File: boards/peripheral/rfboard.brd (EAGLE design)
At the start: 30 x 60 mm, 30 parts, among them Q1 IRLML5203, Q2 IRLML5203, Q3 IRLML5203, Q4 IRLML5203, Q5 IRLML5203

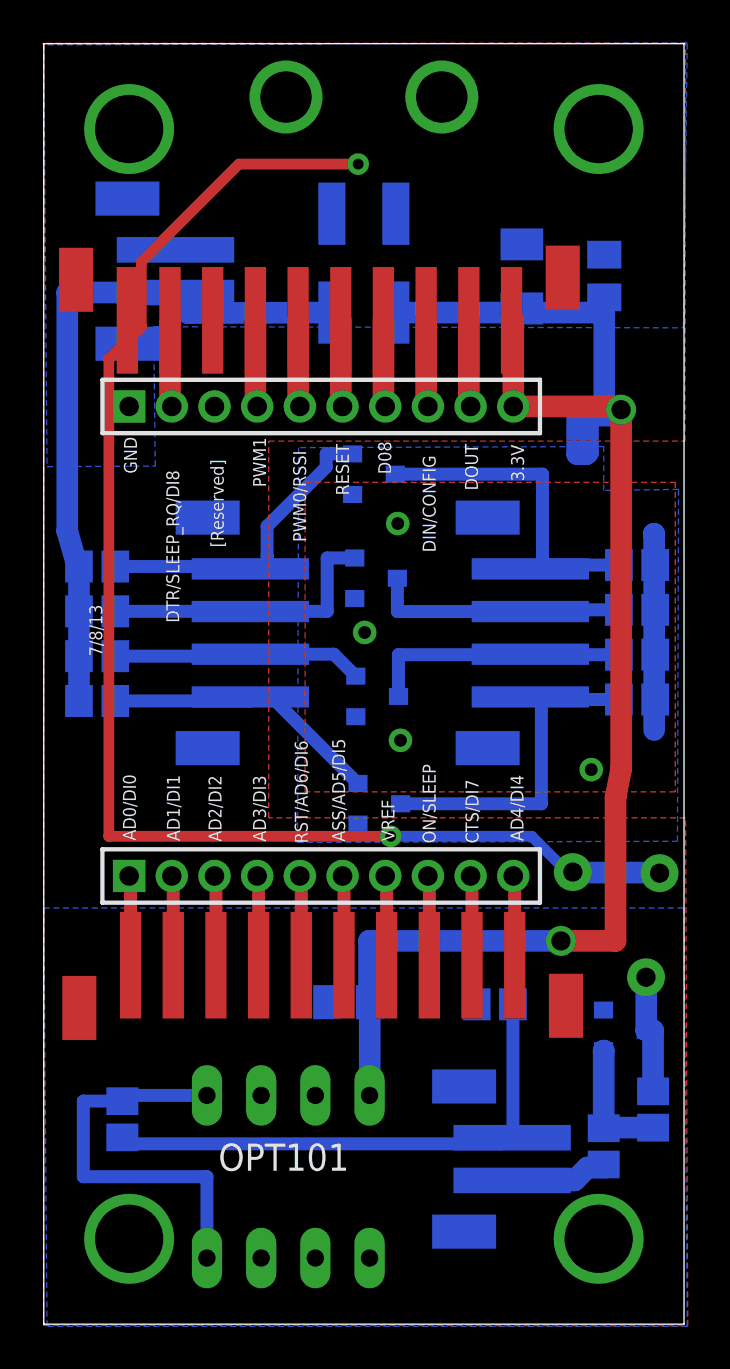
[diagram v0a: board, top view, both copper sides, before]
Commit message: Changing boards for fet and text improvements
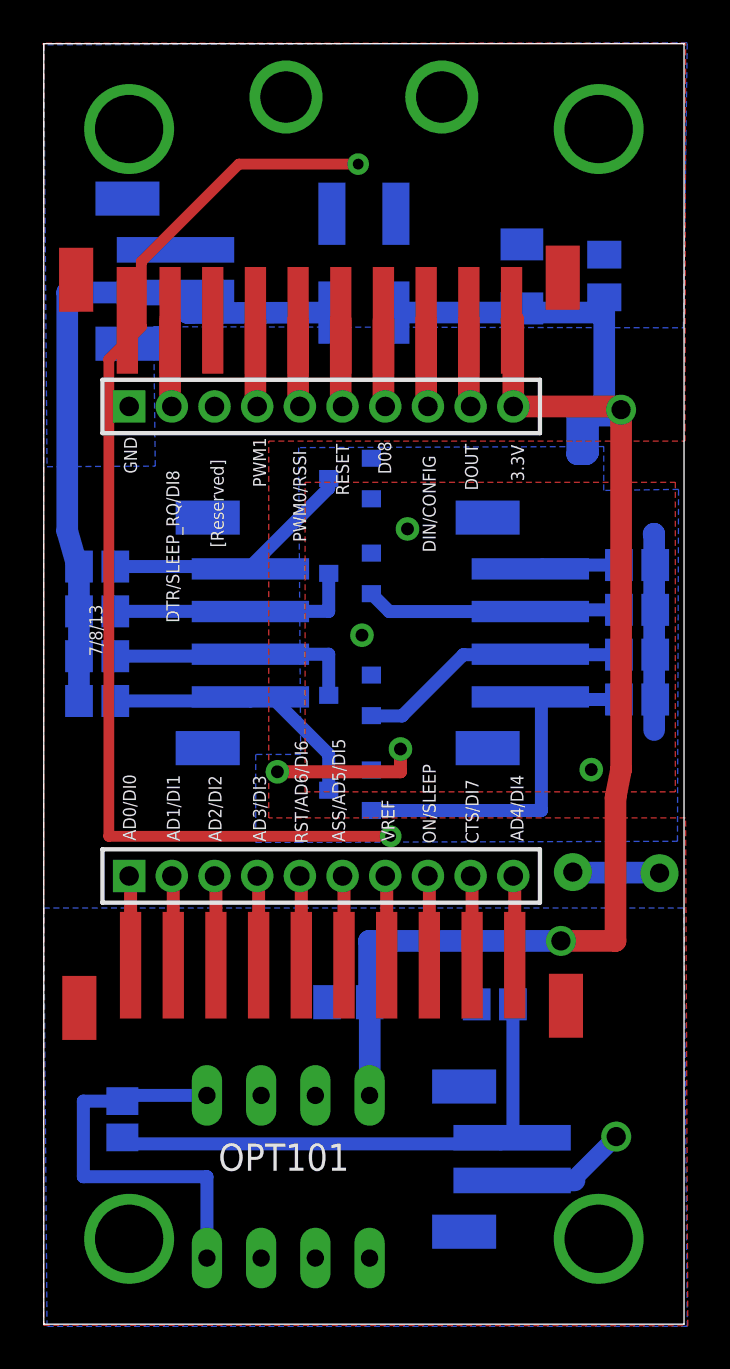
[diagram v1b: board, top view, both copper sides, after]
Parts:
- removed Q5: IRLML5203, ngohara_parts:MICRO3
- removed RGS: 2.2k, resistor:R0805
- removed RIN: 10k, resistor:R0805
- moved Q4 1.51 mm to (14.4, 25.0), turned to 270 degrees
- moved Q3 1.27 mm to (14.4, 29.5), turned to 270 degrees
- moved Q2 1.24 mm to (14.4, 35.2), turned to 270 degrees
- moved Q1 1.14 mm to (14.4, 39.6), turned to 270 degrees
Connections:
- removed net N$2: Q5.1, RGS.1, RIN.2
- net AMB_ON: no longer RIN.1
- net GND: no longer Q5.3, RGS.2
- net H1: now also Q1.3; no longer Q1.2
- net H2: now also Q2.3; no longer Q2.2
- net H3: now also Q3.3; no longer Q3.2
- net H4: now also Q4.3; no longer Q4.2
- net L1: now also Q1.2; no longer Q1.3
- net L2: now also Q2.2; no longer Q2.3
- net L3: now also Q3.2; no longer Q3.3
- net L4: now also Q4.2; no longer Q4.3
- net N_GND: no longer Q5.2
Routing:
- net GND: track 72.3 -> 57.9 mm, vias 5 -> 4
- net L1: track 15.5 -> 4.35 mm
- net 3.3V: track 84.6 -> 91.4 mm, vias 6 -> 7
- net N$2: track 5.96 -> 0.00 mm
- net H1: track 15.0 -> 12.1 mm
- net H2: track 13.7 -> 11.8 mm
- net L4: track 15.8 -> 17.5 mm
- net AMB_ON: track 4.82 -> 5.81 mm, vias 0 -> 1
- net L3: track 12.3 -> 12.8 mm

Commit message: changes for new boards, cleared DRC
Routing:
- net L1: track 4.35 -> 13.2 mm
- net GND: track 57.9 -> 58.1 mm, vias 4 -> 3
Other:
- board text added: "8/6/13"
- board text removed: "7/8/13"
- board text removed: "ABM_ON"
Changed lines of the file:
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@@
 <wire x1="30" y1="0" x2="0" y2="0" width="0" layer="20"/>
 <wire x1="0" y1="60" x2="0" y2="0" width="0" layer="20"/>
-<text x="13.6144" y="7.0104" size="0.6096" layer="26" rot="MR180">ABM_ON</text>
 <text x="16.9926" y="8.4582" size="0.6096" layer="26" rot="MR0">AMB_OUT</text>
-<text x="29.21" y="37.1348" size="0.6096" layer="26" rot="MR0">3.3 Out</text>
-<text x="3.8354" y="37.084" size="0.6096" layer="26" rot="MR0">5V In</text>
-<text x="19.7358" y="41.2496" size="0.6096" layer="25" rot="R270">DOUT</text>
-<text x="18.3642" y="36.1696" size="0.6096" layer="25" rot="R90">DIN/CONFIG</text>
-<text x="16.2814" y="39.8272" size="0.6096" layer="25" rot="R90">D08</text>
-<text x="14.3002" y="38.8366" size="0.6096" layer="25" rot="R90">RESET</text>
-<text x="12.2936" y="36.6522" size="0.6096" layer="25" rot="R90">PWM0/RSSI</text>
-<text x="10.414" y="39.2176" size="0.6096" layer="25" rot="R90">PWM1</text>
-<text x="6.35" y="32.8676" size="0.6096" layer="25" rot="R90">DTR/SLEEP_RQ/DI8</text>
-<text x="4.3688" y="39.8526" size="0.6096" layer="25" rot="R90">GND</text>
-<text x="22.5044" y="39.497" size="0.6096" layer="25" rot="R90">3.3V</text>
-<text x="8.4328" y="36.3982" size="0.6096" layer="25" rot="R90">[Reserved]</text>
-<text x="4.318" y="22.6568" size="0.6096" layer="25" rot="R90">AD0/DI0</text>
-<text x="6.3754" y="22.6314" size="0.6096" layer="25" rot="R90">AD1/DI1</text>
-<text x="8.3312" y="22.606" size="0.6096" layer="25" rot="R90">AD2/DI2</text>
-<text x="10.414" y="22.606" size="0.6096" layer="25" rot="R90">AD3/DI3</text>
-<text x="12.3698" y="22.5298" size="0.6096" layer="25" rot="R90">RST/AD6/DI6</text>
-<text x="14.1224" y="22.606" size="0.6096" layer="25" rot="R90">ASS/AD5/DI5</text>
-<text x="16.4338" y="22.6314" size="0.6096" layer="25" rot="R90">VREF</text>
-<text x="18.3642" y="22.5298" size="0.6096" layer="25" rot="R90">ON/SLEEP</text>
-<text x="20.3708" y="22.5298" size="0.6096" layer="25" rot="R90">CTS/DI7</text>
-<text x="22.479" y="22.6314" size="0.6096" layer="25" rot="R90">AD4/DI4</text>
-<text x="2.7432" y="31.2928" size="0.6096" layer="25" rot="R90">7/8/13</text>
+<text x="29.21" y="37.1348" size="0.8128" layer="26" rot="MR0">3.3 Out</text>
+<text x="3.8354" y="37.084" size="0.8128" layer="26" rot="MR0">5V In</text>
+<text x="19.7358" y="41.2496" size="0.8128" layer="25" rot="R270">DOUT</text>
+<text x="18.7706" y="34.163" size="0.8128" layer="25" rot="R90">DIN/CONFIG</text>
+<text x="16.7386" y="39.243" size="0.8128" layer="25" rot="R90">D08</text>
+<text x="14.7574" y="37.973" size="0.8128" layer="25" rot="R90">RESET</text>
+<text x="12.7508" y="34.8234" size="0.8128" layer="25" rot="R90">PWM0/RSSI</text>
+<text x="10.795" y="38.354" size="0.8128" layer="25" rot="R90">PWM1</text>
+<text x="6.8072" y="29.8196" size="0.8128" layer="25" rot="R90">DTR/SLEEP_RQ/DI8</text>
+<text x="4.7244" y="39.1668" size="0.8128" layer="25" rot="R90">GND</text>
+<text x="22.8854" y="38.7858" size="0.8128" layer="25" rot="R90">3.3V</text>
+<text x="8.8392" y="34.3408" size="0.8128" layer="25" rot="R90">[Reserved]</text>
+<text x="4.318" y="22.6568" size="0.8128" layer="25" rot="R90">AD0/DI0</text>
+<text x="6.3754" y="22.6314" size="0.8128" layer="25" rot="R90">AD1/DI1</text>
+<text x="8.3312" y="22.606" size="0.8128" layer="25" rot="R90">AD2/DI2</text>
+<text x="10.414" y="22.606" size="0.8128" layer="25" rot="R90">AD3/DI3</text>
+<text x="12.6238" y="22.5298" size="0.8128" layer="25" rot="R90">RST/AD6/DI6</text>
+<text x="14.1224" y="22.606" size="0.8128" layer="25" rot="R90">ASS/AD5/DI5</text>
+<text x="16.4338" y="22.6314" size="0.8128" layer="25" rot="R90">VREF</text>
+<text x="18.3642" y="22.5298" size="0.8128" layer="25" rot="R90">ON/SLEEP</text>
+<text x="20.3708" y="22.5298" size="0.8128" layer="25" rot="R90">CTS/DI7</text>
+<text x="22.479" y="22.6314" size="0.8128" layer="25" rot="R90">AD4/DI4</text>
+<text x="2.7432" y="31.2928" size="0.8128" layer="25" rot="R90">8/6/13</text>
 </plain>
 <attributes>
@@
 <elements>
 <element name="C18" library="rcl" package="C1206K" value="10uF" x="22.4036" y="49.0946" smashed="yes" rot="MR90">
-<attribute name="NAME" x="21.4668" y="46.2884" size="0.8128" layer="26" ratio="16" rot="MR180"/>
 <attribute name="VALUE" x="21.0476" y="50.9668" size="0.8128" layer="28" ratio="16" rot="MR270"/>
 </element>
 <element name="C19" library="rcl" package="C0805K" value=".01uF" x="26.2612" y="49.1146" smashed="yes" rot="MR90">
-<attribute name="NAME" x="27.5586" y="48.6902" size="0.8128" layer="26" ratio="16" rot="MR180"/>
-<attribute name="VALUE" x="26.2124" y="47.0964" size="0.8128" layer="28" ratio="16" rot="MR180"/>
+<attribute name="VALUE" x="27.9606" y="47.7008" size="0.8128" layer="28" ratio="16" rot="MR90"/>
 </element>
 <element name="OPT101" library="ic-package" package="DIL08" value="" x="11.4554" y="6.9088" smashed="yes" rot="R180">
-<attribute name="NAME" x="8.1788" y="7.1882" size="1.27" layer="25" ratio="10"/>
+<attribute name="NAME" x="8.6106" y="6.4008" size="1.27" layer="25" ratio="10"/>
 <attribute name="VALUE" x="15.0114" y="7.5438" size="1.27" layer="27" ratio="10" rot="R180"/>
 </element>
 <element name="C1" library="rcl" package="C0805K" value=".01uF" x="14.2748" y="15.0876" smashed="yes" rot="MR0">
-<attribute name="NAME" x="15.1986" y="16.115" size="1.016" layer="26" rot="MR0"/>
 <attribute name="VALUE" x="14.8176" y="13.086" size="1.016" layer="28" rot="MR0"/>
 </element>
@@
 <element name="U$2" library="jst-ph" package="JST-PH2-SMD" value="JST-PH2-SMD" x="17.1958" y="3.7592" rot="MR90"/>
 <element name="AMB1" library="resistor" package="R0805" value="200k" x="3.683" y="9.6012" smashed="yes" rot="MR90">
-<attribute name="VALUE" x="1.1684" y="7.5438" size="1.27" layer="28" rot="MR90"/>
+<attribute name="VALUE" x="1.1684" y="7.5438" size="0.8128" layer="28" rot="MR90"/>
 </element>
 <element name="AMB2" library="resistor" package="R0805" value="96k" x="21.1328" y="14.986" smashed="yes" rot="MR0">
-<attribute name="VALUE" x="22.3012" y="16.0782" size="1.27" layer="28" rot="MR0"/>
+<attribute name="VALUE" x="22.3012" y="16.0782" size="0.8128" layer="28" rot="MR0"/>
 </element>
 <element name="U$1" library="jst-ph" package="JST-PH10-SMD" value="JST-PH10-SMD" x="1.0922" y="12.319"/>
@@
 <wire x1="4.572" y1="49.784" x2="4.572" y2="46.736" width="0.508" layer="1"/>
 <wire x1="9.144" y1="54.356" x2="4.572" y2="49.784" width="0.508" layer="1"/>
-<wire x1="14.732" y1="54.356" x2="9.144" y2="54.356" width="0.508" layer="1"/>
-<wire x1="24.384" y1="21.336" x2="24.7904" y2="21.1836" width="0.508" layer="16"/>
-<via x="16.256" y="22.86" extent="1-16" drill="0.508" alwaysstop="yes"/>
-<via x="14.732" y="54.356" extent="1-16" drill="0.508" alwaysstop="yes"/>
-<wire x1="24.7904" y1="21.1582" x2="24.7904" y2="21.1836" width="0" layer="19" extent="16-16"/>
+<wire x1="15.3162" y1="55.2704" x2="9.144" y2="54.356" width="0.508" layer="1"/>
+<via x="15.3162" y="55.2704" extent="1-16" drill="0.508" alwaysstop="yes"/>
+<wire x1="24.7904" y1="21.1582" x2="24.7904" y2="21.1836" width="0.6096" layer="16"/>
 </signal>
 <signal name="AMB_OUT">
@@
 <via x="16.7132" y="26.9494" extent="1-16" drill="0.6" alwaysstop="yes"/>
 <via x="25.654" y="25.9842" extent="1-16" drill="0.6" alwaysstop="yes"/>
-<via x="17.0434" y="37.2618" extent="1-16" drill="0.6" alwaysstop="yes"/>
+<via x="13.6906" y="37.338" extent="1-16" drill="0.6" alwaysstop="yes"/>
 <via x="14.9098" y="32.2834" extent="1-16" drill="0.6" alwaysstop="yes"/>
 <wire x1="22.86" y1="47.752" x2="22.4036" y2="47.5946" width="0.508" layer="16"/>
 <wire x1="22.86" y1="47.752" x2="22.86" y2="47.4" width="0.508" layer="16"/>
-<via x="10.9474" y="25.8826" extent="1-16" drill="0.6" alwaysstop="yes"/>
+<via x="11.1252" y="25.908" extent="1-16" drill="0.6" alwaysstop="yes"/>
 <wire x1="16.7132" y1="26.9494" x2="16.7132" y2="25.8826" width="0.6096" layer="1"/>
-<wire x1="16.7132" y1="25.8826" x2="10.9474" y2="25.8826" width="0.6096" layer="1"/>
+<wire x1="16.7132" y1="25.8826" x2="11.1252" y2="25.908" width="0.6096" layer="1"/>
 </signal>
 <signal name="5V" class="1">
@@
 <wire x1="26.95" y1="35.5698" x2="23.368" y2="35.5698" width="0.6096" layer="16"/>
 <wire x1="23.368" y1="35.5698" x2="23.368" y2="35.3822" width="0.6096" layer="16"/>
-<wire x1="22.8" y1="35.391" x2="15.351" y2="38.674" width="0" layer="19" extent="16-16"/>
+<wire x1="22.8" y1="35.391" x2="18.634" y2="35.391" width="0.6096" layer="16"/>
+<wire x1="18.634" y1="35.391" x2="15.351" y2="38.674" width="0.6096" layer="16"/>
 </signal>
 </signals>
